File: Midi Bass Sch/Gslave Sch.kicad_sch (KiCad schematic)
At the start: 5 parts

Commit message: updated e slave added solenoid for slave added reset button
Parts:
- gave numbers to parts that had none: 5
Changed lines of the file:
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@@
 		(dnp no)
 		(fields_autoplaced yes)
-		(property "Reference" "R?"
+		(property "Reference" "R19"
 			(at 83.82 124.4599 90)
 			(effects
@@
 			(project "Midi Bass Sch"
 				(path "/06818073-fb22-48ee-acc5-6dedd827034e/a79027be-e76c-43a0-a80a-a6c6a159c340"
-					(reference "R?")
+					(reference "R19")
 					(unit 1)
 				)
@@
 		(dnp no)
 		(fields_autoplaced yes)
-		(property "Reference" "U?"
+		(property "Reference" "U7"
 			(at 154.5941 152.4 0)
 			(effects
@@
 			(project "Midi Bass Sch"
 				(path "/06818073-fb22-48ee-acc5-6dedd827034e/a79027be-e76c-43a0-a80a-a6c6a159c340"
-					(reference "U?")
+					(reference "U7")
 					(unit 1)
 				)
@@
 		(dnp no)
 		(fields_autoplaced yes)
-		(property "Reference" "D?"
+		(property "Reference" "D9"
 			(at 93.98 125.73 90)
 			(effects
@@
 			(project "Midi Bass Sch"
 				(path "/06818073-fb22-48ee-acc5-6dedd827034e/a79027be-e76c-43a0-a80a-a6c6a159c340"
-					(reference "D?")
+					(reference "D9")
 					(unit 1)
 				)
@@
 		(dnp no)
 		(fields_autoplaced yes)
-		(property "Reference" "TP?"
+		(property "Reference" "TP9"
 			(at 89.408 64.77 90)
 			(effects
@@
 			(project "Midi Bass Sch"
 				(path "/06818073-fb22-48ee-acc5-6dedd827034e/a79027be-e76c-43a0-a80a-a6c6a159c340"
-					(reference "TP?")
+					(reference "TP9")
 					(unit 1)
 				)
@@
 		(dnp no)
 		(fields_autoplaced yes)
-		(property "Reference" "C?"
+		(property "Reference" "C6"
 			(at 83.82 135.2549 0)
 			(effects
@@
 			(project "Midi Bass Sch"
 				(path "/06818073-fb22-48ee-acc5-6dedd827034e/a79027be-e76c-43a0-a80a-a6c6a159c340"
-					(reference "C?")
-					(unit 1)
-				)
+					(reference "C6")
+					(unit 1)
+				)

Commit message: added solenoid array for the A slave
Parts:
- renumbered D9 to D18, R19 to R51, U7 to U8
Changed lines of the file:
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@@
 	(generator "eeschema")
 	(generator_version "8.0")
-	(paper "A4")
+	(paper "A")
 	(junction
 		(at 138.43 25.4)
@@
 		(dnp no)
 		(fields_autoplaced yes)
-		(property "Reference" "#PWR041"
+		(property "Reference" "#PWR070"
 			(at 86.0044 116.9416 0)
 			(effects
@@
 			(project "Midi Bass Sch"
 				(path "/06818073-fb22-48ee-acc5-6dedd827034e/a79027be-e76c-43a0-a80a-a6c6a159c340"
-					(reference "#PWR041")
+					(reference "#PWR070")
 					(unit 1)
 				)
@@
 		(dnp no)
 		(fields_autoplaced yes)
-		(property "Reference" "R19"
+		(property "Reference" "R51"
 			(at 83.82 124.4599 90)
 			(effects
@@
 			(project "Midi Bass Sch"
 				(path "/06818073-fb22-48ee-acc5-6dedd827034e/a79027be-e76c-43a0-a80a-a6c6a159c340"
-					(reference "R19")
+					(reference "R51")
 					(unit 1)
 				)
@@
 		(dnp no)
 		(fields_autoplaced yes)
-		(property "Reference" "U7"
+		(property "Reference" "U8"
 			(at 154.5941 152.4 0)
 			(effects
@@
 			(project "Midi Bass Sch"
 				(path "/06818073-fb22-48ee-acc5-6dedd827034e/a79027be-e76c-43a0-a80a-a6c6a159c340"
-					(reference "U7")
+					(reference "U8")
 					(unit 1)
 				)
@@
 		(dnp no)
 		(fields_autoplaced yes)
-		(property "Reference" "#PWR042"
+		(property "Reference" "#PWR071"
 			(at 81.28 138.43 0)
 			(effects
@@
 			(project "Midi Bass Sch"
 				(path "/06818073-fb22-48ee-acc5-6dedd827034e/a79027be-e76c-43a0-a80a-a6c6a159c340"
-					(reference "#PWR042")
+					(reference "#PWR071")
 					(unit 1)
 				)
@@
 		(dnp no)
 		(fields_autoplaced yes)
-		(property "Reference" "#PWR044"
+		(property "Reference" "#PWR073"
 			(at 143.51 154.94 0)
 			(effects
@@
 			(project "Midi Bass Sch"
 				(path "/06818073-fb22-48ee-acc5-6dedd827034e/a79027be-e76c-43a0-a80a-a6c6a159c340"
-					(reference "#PWR044")
+					(reference "#PWR073")
 					(unit 1)
 				)
@@
 		(dnp no)
 		(fields_autoplaced yes)
-		(property "Reference" "D9"
+		(property "Reference" "D18"
 			(at 93.98 125.73 90)
 			(effects
@@
 			(project "Midi Bass Sch"
 				(path "/06818073-fb22-48ee-acc5-6dedd827034e/a79027be-e76c-43a0-a80a-a6c6a159c340"
-					(reference "D9")
+					(reference "D18")
 					(unit 1)
 				)
@@
 		(dnp no)
 		(fields_autoplaced yes)
-		(property "Reference" "#PWR043"
+		(property "Reference" "#PWR072"
 			(at 143.1544 20.4216 0)
 			(effects
@@
 			(project "Midi Bass Sch"
 				(path "/06818073-fb22-48ee-acc5-6dedd827034e/a79027be-e76c-43a0-a80a-a6c6a159c340"
-					(reference "#PWR043")
+					(reference "#PWR072")
 					(unit 1)
 				)

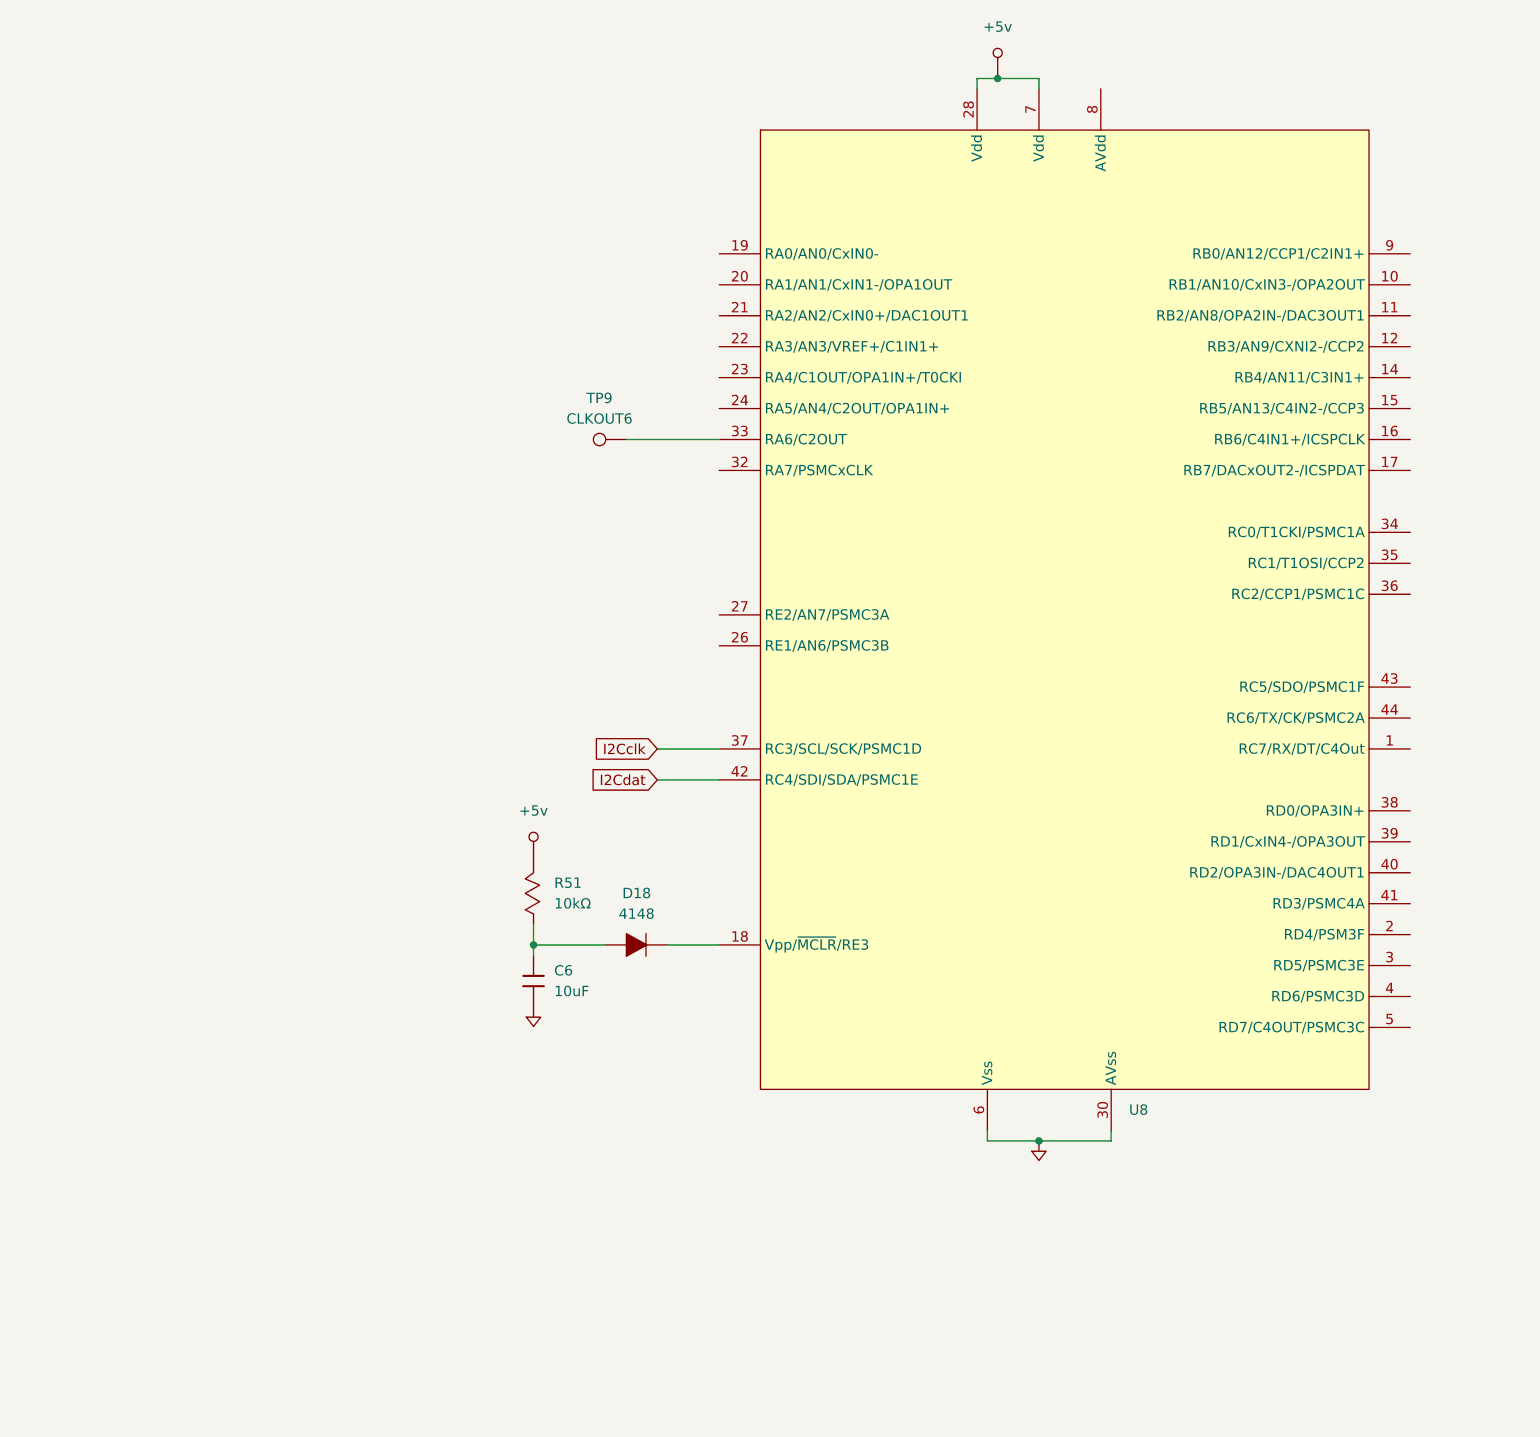
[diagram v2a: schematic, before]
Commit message: added solenoid array for the G slave
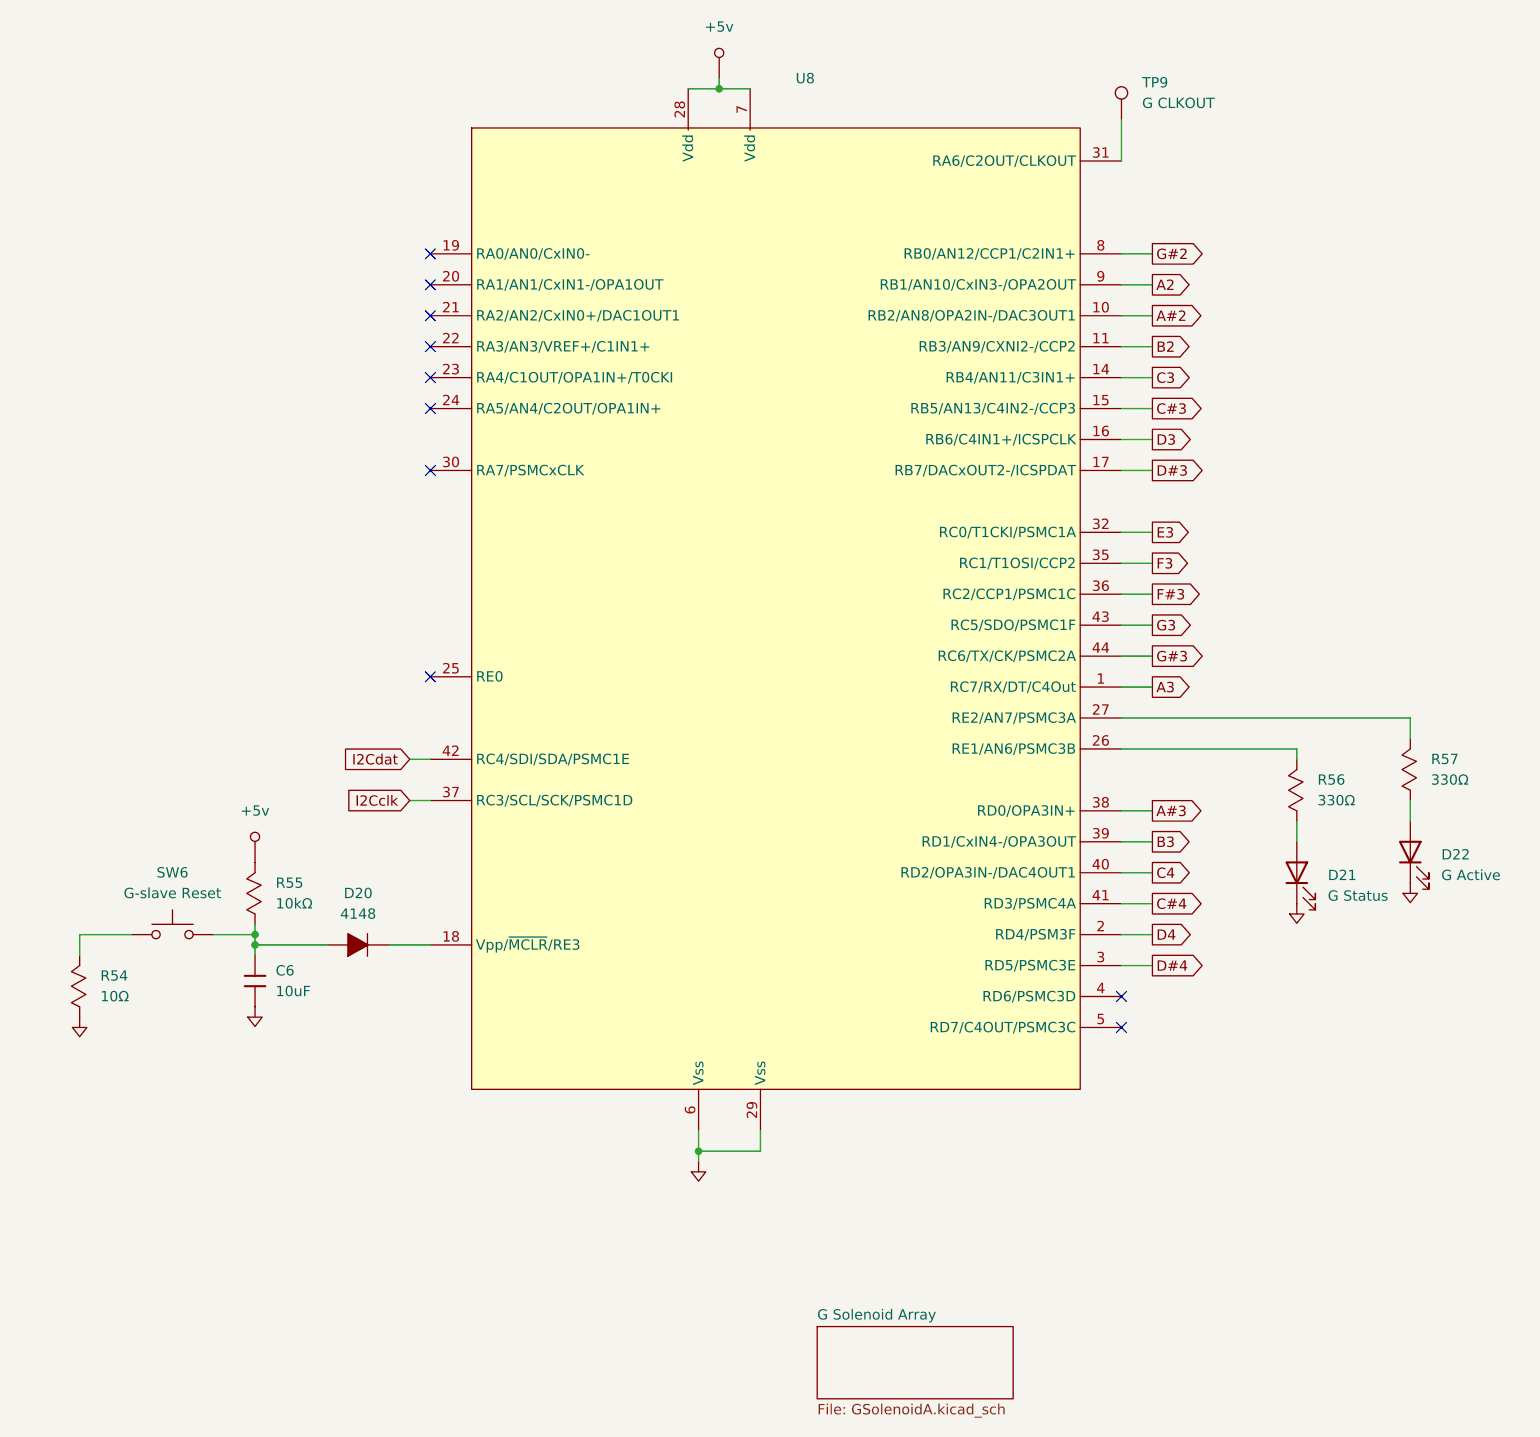
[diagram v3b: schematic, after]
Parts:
- removed D18: 4148, symbol Owen's Symbols:Diode
- removed R51: 10kΩ, symbol Owen's Symbols:Resistor_Mod
- added D20: 4148, symbol Owen's Symbols:Diode
- added D21: G Status, symbol Device:LED
- added D22: G Active, symbol Device:LED
- added R54: 10Ω, symbol Owen's Symbols:Resistor_Mod
- added R55: 10kΩ, symbol Owen's Symbols:Resistor_Mod
- added R56, R57: 330Ω, symbol Owen's Symbols:Resistor_Mod
- added SW6: G-slave Reset, symbol Switch:SW_Push
- TP9: value CLKOUT6 -> G CLKOUT
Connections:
- net +5v: now also R55.2
- net GND: now also U8.29 (Vss), D21.1 (K), D22.1 (K), R54.1; no longer U8.30 (AVss)
- net at C6.1: now also D20.1, R55.1, SW6.2
- net at U8.1 (RC7/RX/DT/C4Out): now also R56.2
- net A#2: now reaches U8.10 (RB2/AN8/OPA2IN-/DAC3OUT1)
- net B2: now reaches U8.11 (RB3/AN9/CXNI2-/CCP2)
- net C3: now reaches U8.14 (RB4/AN11/C3IN1+)
- net C#3: now reaches U8.15 (RB5/AN13/C4IN2-/CCP3)
- net D3: now reaches U8.16 (RB6/C4IN1+/ICSPCLK)
- net D#3: now reaches U8.17 (RB7/DACxOUT2-/ICSPDAT)
- net at U8.18 (Vpp/~{MCLR}/RE3): now also D20.2
- net D4: now reaches U8.2 (RD4/PSM3F)
- net D#4: now reaches U8.3 (RD5/PSMC3E)
- net E3: now reaches U8.32 (RC0/T1CKI/PSMC1A)
- net at TP9.1: now also U8.31 (RA6/C2OUT/CLKOUT); no longer U8.33 (RA6/C2OUT)
- net F3: now reaches U8.35 (RC1/T1OSI/CCP2)
- net F#3: now reaches U8.36 (RC2/CCP1/PSMC1C)
- net G3: now reaches U8.37 (RC3/SCL/SCK/PSMC1D)
- net A#3: now reaches U8.38 (RD0/OPA3IN+)
- net B3: now reaches U8.39 (RD1/CxIN4-/OPA3OUT)
- net C4: now reaches U8.40 (RD2/OPA3IN-/DAC4OUT1)
- net C#4: now reaches U8.41 (RD3/PSMC4A)
- net G#3: now reaches U8.42 (RC4/SDI/SDA/PSMC1E)
- net A3: now reaches U8.43 (RC5/SDO/PSMC1F)
- net at U8.44 (RC6/TX/CK/PSMC2A): now also R57.2
- net G#2: now reaches U8.8 (RB0/AN12/CCP1/C2IN1+)
- net A2: now reaches U8.9 (RB1/AN10/CxIN3-/OPA2OUT)
- new net: D21.2 (A), R56.1
- new net: D22.2 (A), R57.1
- new net: R54.2, SW6.1
- no-connect marks 0 -> 10
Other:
- added sheet G Solenoid Array (GSolenoidA.kicad_sch)

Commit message: added program pins to all processors
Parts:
- added J?: G SLAVE ISCP, symbol Owen's Symbols:Header_1x6
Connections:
- net +5v: now also J?.2
- net D#3: now also J?.4
- net D3: now also J?.5
- net GND: now also J?.3
- net MSCLR G: now reaches D20.2, U8.18 (Vpp/~{MCLR}/RE3)
- net MSCLR G: now also J?.1
- no-connect marks 10 -> 11

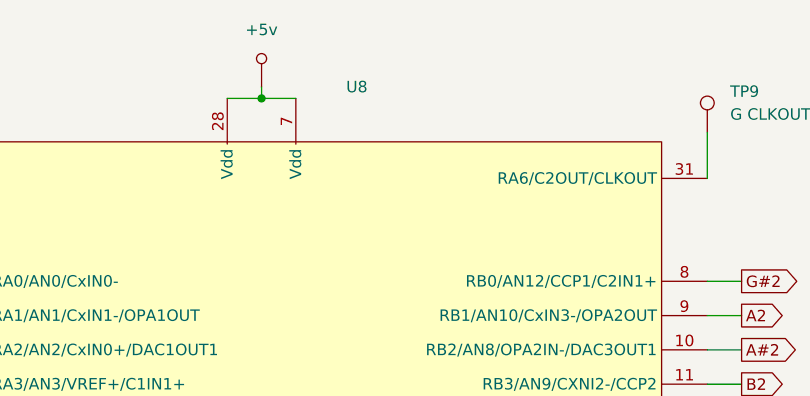
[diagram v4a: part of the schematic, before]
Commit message: added footprints to kicad schematic still need footprint for din connector
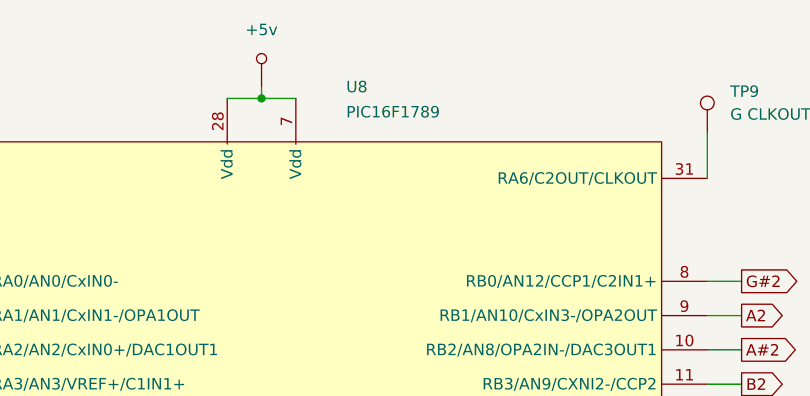
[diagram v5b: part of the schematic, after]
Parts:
- C6: footprint (none) -> Capacitor_SMD:C_0805_2012Metric_Pad1.18x1.45mm_HandSolder
- D20, D21, D22: footprint (none) -> Diode_SMD:D_0805_2012Metric_Pad1.15x1.40mm_HandSolder
- J?: footprint (none) -> Connector_PinHeader_2.54mm:PinHeader_1x06_P2.54mm_Vertical
- R54, R55, R56, R57: footprint (none) -> Resistor_SMD:R_0805_2012Metric_Pad1.20x1.40mm_HandSolder
- U8: value ~ -> PIC16F1789
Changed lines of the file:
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@@
 			)
 		)
-		(property "Footprint" ""
+		(property "Footprint" "Resistor_SMD:R_0805_2012Metric_Pad1.20x1.40mm_HandSolder"
 			(at 172.72 114.3 0)
 			(effects
@@
 			)
 		)
-		(property "Footprint" ""
+		(property "Footprint" "Resistor_SMD:R_0805_2012Metric_Pad1.20x1.40mm_HandSolder"
 			(at 44.45 127 0)
 			(effects
@@
 			)
 		)
-		(property "Footprint" ""
+		(property "Footprint" "Connector_PinHeader_2.54mm:PinHeader_1x06_P2.54mm_Vertical"
 			(at 25.4 50.8 0)
 			(effects
@@
 			)
 		)
-		(property "Footprint" ""
+		(property "Footprint" "Diode_SMD:D_0805_2012Metric_Pad1.15x1.40mm_HandSolder"
 			(at 189.23 120.65 0)
 			(effects
@@
 			)
 		)
-		(property "Footprint" ""
+		(property "Footprint" "Resistor_SMD:R_0805_2012Metric_Pad1.20x1.40mm_HandSolder"
 			(at 186.69 111.76 0)
 			(effects
@@
 			)
 		)
-		(property "Footprint" ""
+		(property "Footprint" "Capacitor_SMD:C_0805_2012Metric_Pad1.18x1.45mm_HandSolder"
 			(at 46.99 130.81 0)
 			(effects
@@
 			)
 		)
-		(property "Value" "~"
-			(at 119.0341 153.67 0)
+		(property "Value" "PIC16F1789"
+			(at 113.538 28.194 0)
 			(effects
 				(font
@@
 			)
 		)
-		(property "Footprint" ""
+		(property "Footprint" "Diode_SMD:D_0805_2012Metric_Pad1.15x1.40mm_HandSolder"
 			(at 55.88 132.08 0)
 			(effects
@@
 			)
 		)
-		(property "Footprint" ""
+		(property "Footprint" "Diode_SMD:D_0805_2012Metric_Pad1.15x1.40mm_HandSolder"
 			(at 175.26 123.19 0)
 			(effects
@@
 			)
 		)
-		(property "Footprint" ""
+		(property "Footprint" "Resistor_SMD:R_0805_2012Metric_Pad1.20x1.40mm_HandSolder"
 			(at 22.86 138.43 0)
 			(effects
